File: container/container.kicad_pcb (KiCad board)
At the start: 2 copper layers, 94 x 94 mm, 422 parts, among them SW1 SW_PUSH, SW10 SW_PUSH, SW11 SW_PUSH, SW12 SW_PUSH, SW13 SW_PUSH, SW14 SW_PUSH, SW15 SW_PUSH, SW16 SW_PUSH, SW17 SW_PUSH, SW18 SW_PUSH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

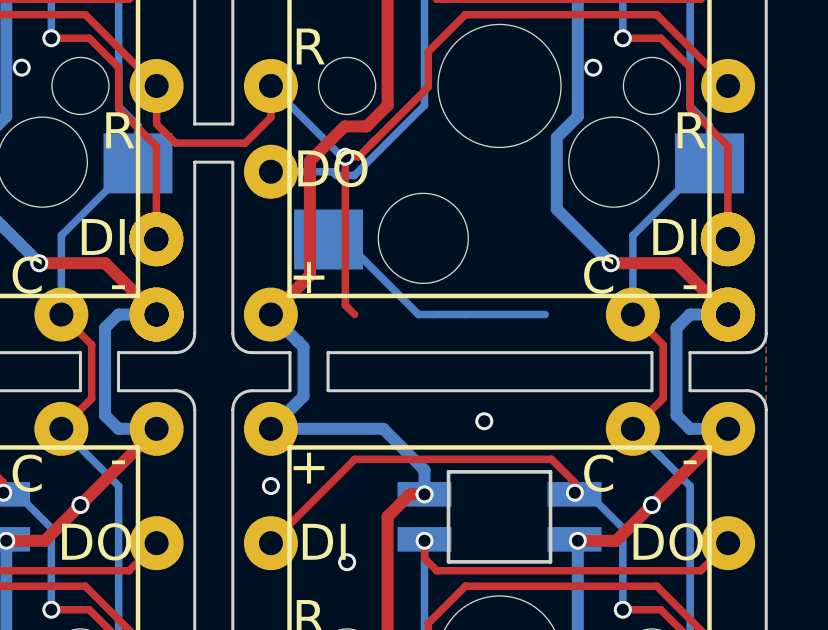
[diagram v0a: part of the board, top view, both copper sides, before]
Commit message: update large silk and forgot diode
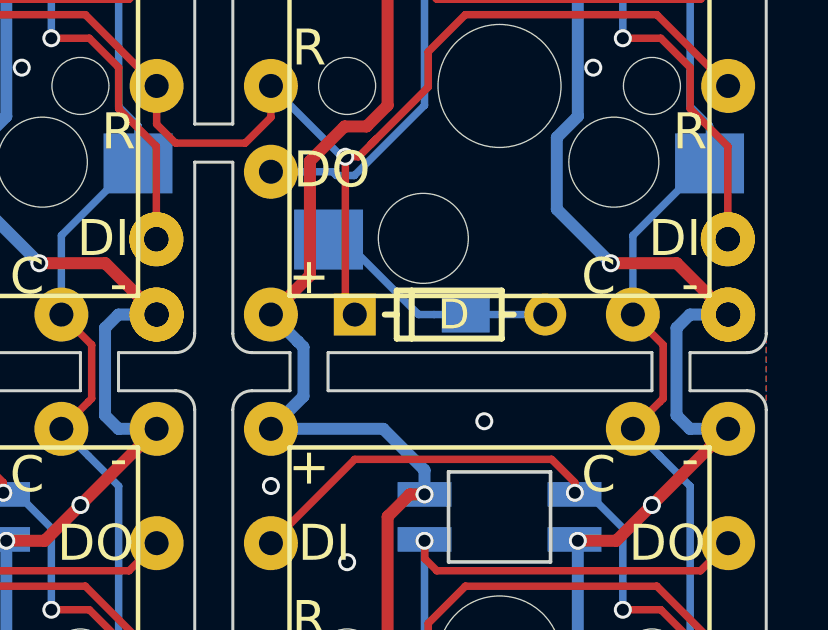
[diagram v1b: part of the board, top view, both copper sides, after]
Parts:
- added D: D, keyboard:D3_hybrid_common_hole, F.Cu at (145.8, 81.4)

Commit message: fix silk
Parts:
- L1 (x25): footprint keyboard:YS-SK6812MINI-E -> Keyboard:YS-SK6812MINI-E
